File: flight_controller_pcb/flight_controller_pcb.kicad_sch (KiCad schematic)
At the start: 52 parts, among them J1 Conn_01x08, J2 Conn_01x05, J3 Conn_01x02, U1 NRF24L01P-R7, U2 TPS62162DSG, U3 STM32F411CEUx, U4 RFX2401C, U5 BMP390, U6 MPU-6500, U7 2450LP14A0100001T, Y1 Crystal_GND24

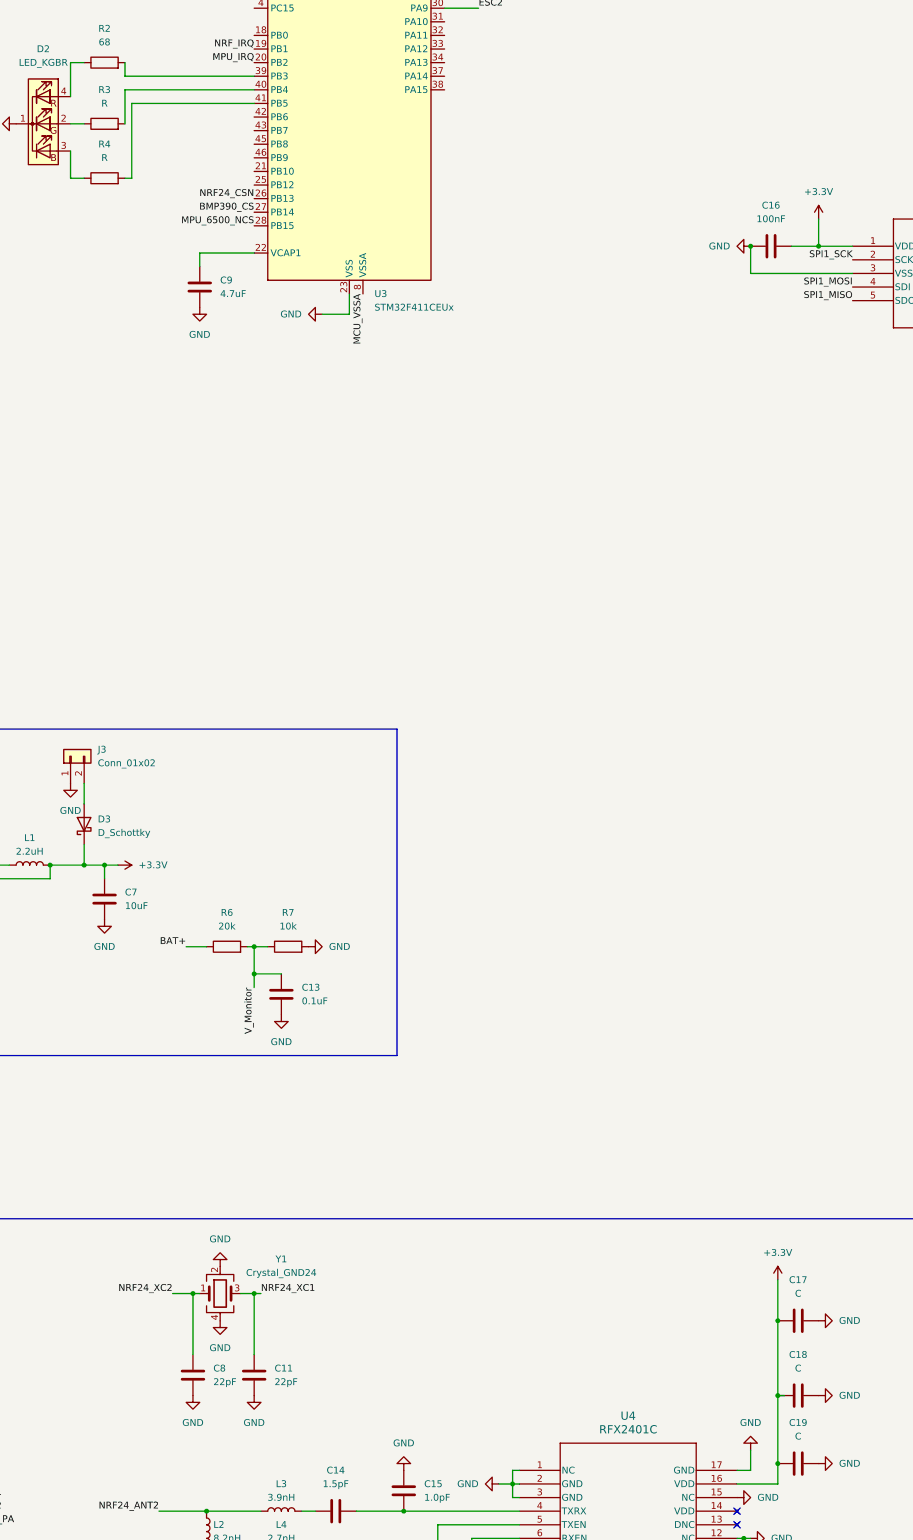
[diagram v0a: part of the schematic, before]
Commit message: assigned several footprints in FC schema
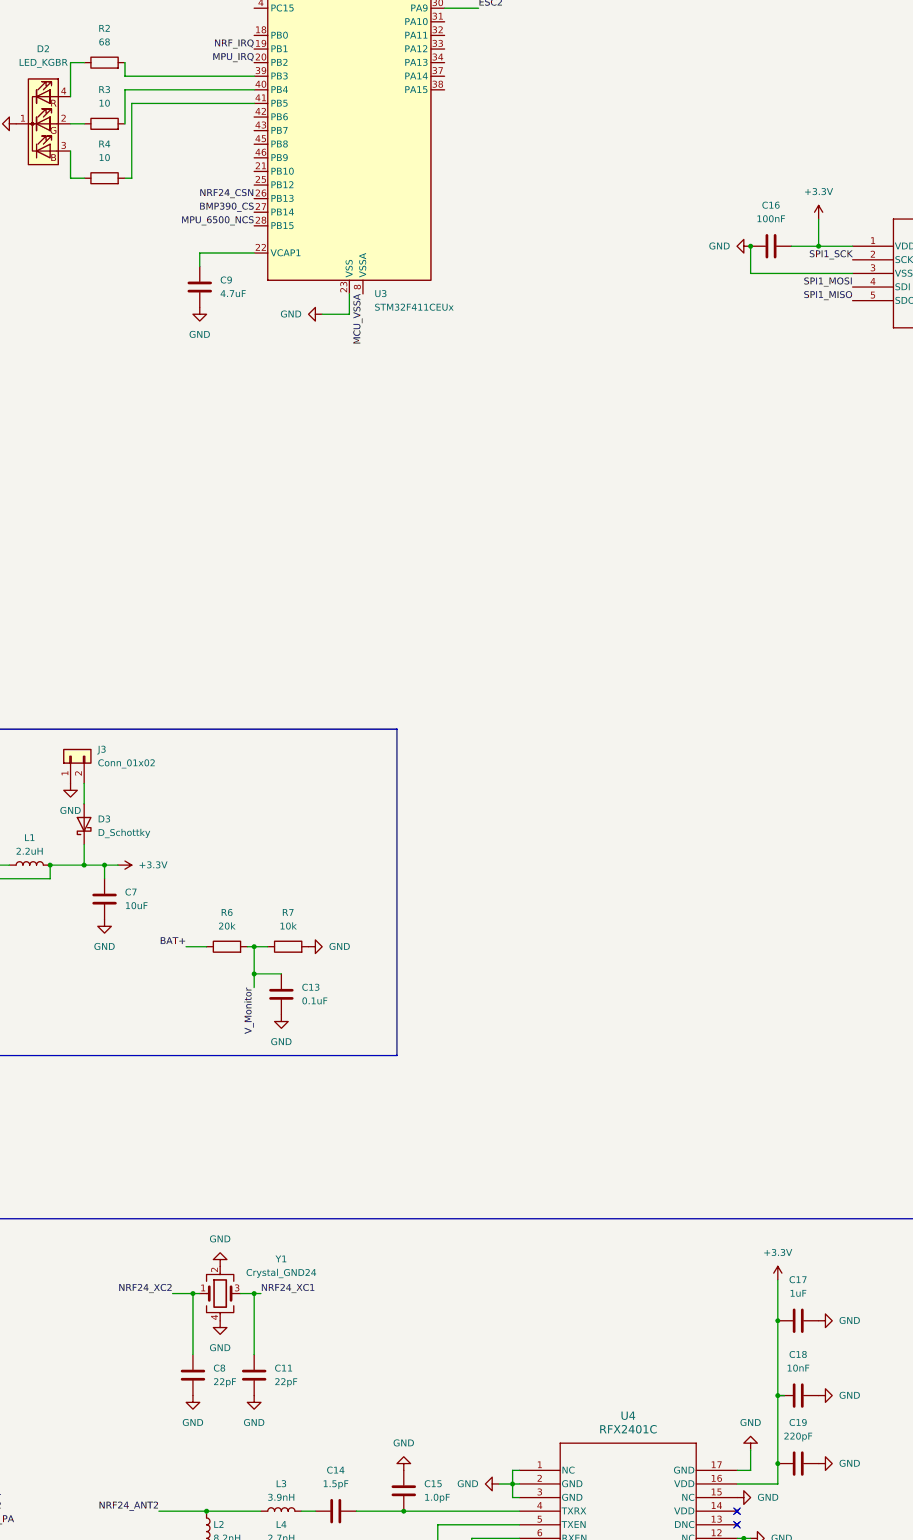
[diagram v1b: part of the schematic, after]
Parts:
- C14, C15, C5, C6: footprint (none) -> Capacitor_SMD:C_0402_1005Metric
- C17: value C -> 1uF; footprint (none) -> Capacitor_SMD:C_0402_1005Metric
- C18: value C -> 10nF; footprint (none) -> Capacitor_SMD:C_0603_1608Metric
- C19: value C -> 220pF; footprint (none) -> Capacitor_SMD:C_0402_1005Metric
- C20: footprint (none) -> Capacitor_SMD:C_0201_0603Metric
- C9: footprint (none) -> Capacitor_SMD:C_0603_1608Metric
- L3, L4: footprint (none) -> Inductor_SMD:L_0201_0603Metric
- R2, R5, R8, R9: footprint (none) -> Resistor_SMD:R_0402_1005Metric
- R3, R4: value R -> 10; footprint (none) -> Resistor_SMD:R_0402_1005Metric
- TP1: footprint (none) -> TestPoint:TestPoint_Pad_3.0x3.0mm
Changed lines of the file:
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@@
 			)
 		)
-		(property "Footprint" ""
+		(property "Footprint" "Capacitor_SMD:C_0201_0603Metric"
 			(at 229.5652 386.08 0)
 			(effects
@@
 			)
 		)
-		(property "Description" "Unpolarized capacitor"
+		(property "Description" "Unpolarized capacitor (C180283)"
 			(at 228.6 382.27 0)
 			(effects
@@
 			)
 		)
-		(property "Value" "R"
+		(property "Value" "10"
 			(at 95.25 105.41 90)
 			(effects
@@
 			)
 		)
-		(property "Footprint" ""
+		(property "Footprint" "Resistor_SMD:R_0402_1005Metric"
 			(at 95.25 110.998 90)
 			(effects
@@
 			)
 		)
-		(property "Description" "Resistor"
+		(property "Description" "Resistor (C25077)"
 			(at 95.25 109.22 0)
 			(effects
@@
 			)
 		)
-		(property "Footprint" ""
+		(property "Footprint" "TestPoint:TestPoint_Pad_3.0x3.0mm"
 			(at 290.83 383.54 0)
 			(effects
@@
 			)
 		)
-		(property "Footprint" ""
+		(property "Footprint" "Capacitor_SMD:C_0402_1005Metric"
 			(at 77.1652 50.8 0)
 			(effects
@@
 			)
 		)
-		(property "Description" "Unpolarized capacitor"
+		(property "Description" "Unpolarized capacitor (C52923)"
 			(at 76.2 46.99 0)
 			(effects
@@
 			)
 		)
-		(property "Footprint" ""
+		(property "Footprint" "Capacitor_SMD:C_0603_1608Metric"
 			(at 112.0648 135.89 0)
 			(effects
@@
 			)
 		)
-		(property "Description" "Unpolarized capacitor (MLCC, low ERS < 1ohm)"
+		(property "Description" "Unpolarized capacitor (C107368)"
 			(at 113.03 139.7 0)
 			(effects
@@
 			)
 		)
-		(property "Footprint" ""
+		(property "Footprint" "Resistor_SMD:R_0402_1005Metric"
 			(at 95.25 99.568 90)
 			(effects
@@
 			)
 		)
-		(property "Description" "Resistor"
+		(property "Description" "Resistor (C163455)"
 			(at 95.25 97.79 0)
 			(effects
@@
 			)
 		)
-		(property "Footprint" ""
+		(property "Footprint" "Resistor_SMD:R_0402_1005Metric"
 			(at 162.052 379.73 90)
 			(effects
@@
 			)
 		)
-		(property "Description" "Resistor"
+		(property "Description" "Resistor (C11702)"
 			(at 163.83 379.73 0)
 			(effects
@@
 			)
 		)
-		(property "Value" "C"
+		(property "Value" "10nF"
 			(at 224.79 341.63 90)
 			(effects
@@
 			)
 		)
-		(property "Footprint" ""
+		(property "Footprint" "Capacitor_SMD:C_0603_1608Metric"
 			(at 228.6 345.7448 0)
 			(effects
@@
 			)
 		)
-		(property "Description" "Unpolarized capacitor"
+		(property "Description" "Unpolarized capacitor (C389113)"
 			(at 224.79 346.71 0)
 			(effects
@@
 			)
 		)
-		(property "Footprint" ""
+		(property "Footprint" "Resistor_SMD:R_0402_1005Metric"
 			(at 104.902 73.66 90)
 			(effects
@@
 			)
 		)
-		(property "Description" "Resistor"
+		(property "Description" "Resistor (C25744)"
 			(at 106.68 73.66 0)
 			(effects
@@
 			)
 		)
-		(property "Footprint" ""
+		(property "Footprint" "Inductor_SMD:L_0201_0603Metric"
 			(at 128.27 375.92 0)
 			(effects
@@
 			)
 		)
-		(property "Description" "Inductor (chip inductor +/- 5%)"
+		(property "Description" "Inductor (C98043)"
 			(at 128.27 375.92 0)
 			(effects
@@
 			)
 		)
-		(property "Footprint" ""
+		(property "Footprint" "Inductor_SMD:L_0201_0603Metric"
 			(at 128.27 368.3 0)
 			(effects
@@
 			)
 		)
-		(property "Description" "Inductor"
+		(property "Description" "Inductor (C918993)"
 			(at 128.27 368.3 0)
 			(effects
@@
 			)
 		)
-		(property "Footprint" ""
+		(property "Footprint" "Capacitor_SMD:C_0402_1005Metric"
 			(at 152.0952 368.3 0)
 			(effects
@@
 			)
 		)
-		(property "Description" "Unpolarized capacitor (NPO, +/- 0.1pF)"
+		(property "Description" "Unpolarized capacitor (C309455)"
+			(at 151.13 364.49 0)
+			(effects
+				(font
+					(size 1.27 1.27)
+				)
+				(hide yes)
+			)
+		)
+		(property "Field5" ""
 			(at 151.13 364.49 0)
 			(effects
@@
 			)
 		)
-		(property "Footprint" ""
+		(property "Footprint" "Capacitor_SMD:C_0402_1005Metric"
 			(at 142.24 367.3348 0)
 			(effects
@@
 			)
 		)
-		(property "Description" "Unpolarized capacitor (NPO, +/- 0.1pF)"
+		(property "Description" "Unpolarized capacitor (C282238)"
 			(at 138.43 368.3 0)
 			(effects
@@
 			)
 		)
-		(property "Value" "R"
+		(property "Value" "10"
 			(at 95.25 115.57 90)
 			(effects
@@
 			)
 		)
-		(property "Footprint" ""
+		(property "Footprint" "Resistor_SMD:R_0402_1005Metric"
 			(at 95.25 121.158 90)
 			(effects
@@
 			)
 		)
-		(property "Description" "Resistor"
+		(property "Description" "Resistor (C25077)"
 			(at 95.25 119.38 0)
 			(effects
@@
 			)
 		)
-		(property "Footprint" ""
+		(property "Footprint" "Capacitor_SMD:C_0402_1005Metric"
 			(at 88.5952 50.8 0)
 			(effects
@@
 			)
 		)
-		(property "Description" "Unpolarized capacitor"
+		(property "Description" "Unpolarized capacitor (C15195)"
 			(at 87.63 46.99 0)
 			(effects
@@
 			)
 		)
-		(property "Description" "Inductor (C76778)"
+		(property "Description" "Inductor (C404576)"
 			(at 114.3 372.11 0)
 			(effects
@@
 			)
 		)
-		(property "Footprint" ""
+		(property "Footprint" "Resistor_SMD:R_0402_1005Metric"
 			(at 155.702 387.35 90)
 			(effects
@@
 			)
 		)
-		(property "Description" "Resistor"
+		(property "Description" "Resistor (C11702)"
 			(at 157.48 387.35 0)
 			(effects
@@
 			)
 		)
-		(property "Value" "C"
+		(property "Value" "220pF"
 			(at 224.79 354.33 90)
 			(effects
@@
 			)
 		)
-		(property "Footprint" ""
+		(property "Footprint" "Capacitor_SMD:C_0402_1005Metric"
 			(at 228.6 358.4448 0)
 			(effects
@@
 			)
 		)
-		(property "Description" "Unpolarized capacitor"
+		(property "Description" "Unpolarized capacitor (C326765)"
 			(at 224.79 359.41 0)
 			(effects
@@
 			)
 		)
-		(property "Value" "C"
+		(property "Value" "1uF"
 			(at 224.79 327.66 90)
 			(effects
@@
 			)
 		)
-		(property "Footprint" ""
+		(property "Footprint" "Capacitor_SMD:C_0402_1005Metric"
 			(at 228.6 331.7748 0)
 			(effects
@@
 			)
 		)
-		(property "Description" "Unpolarized capacitor"
+		(property "Description" "Unpolarized capacitor (C52923)"
 			(at 224.79 332.74 0)
 			(effects

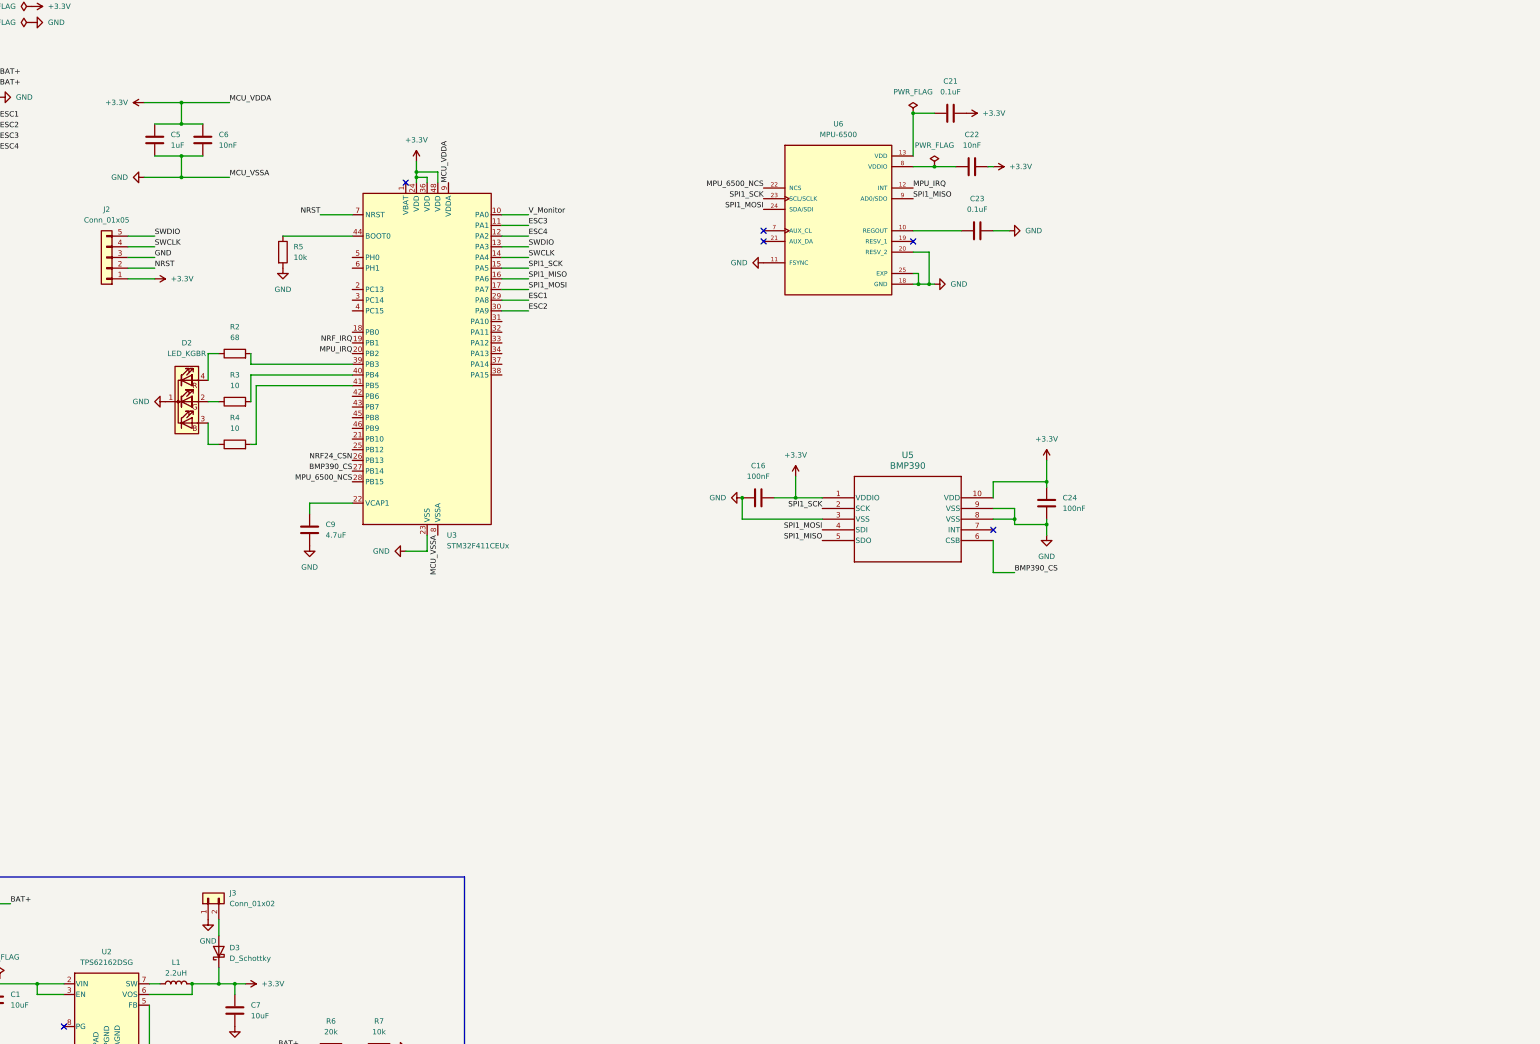
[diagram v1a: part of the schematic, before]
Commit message: Started work to replace mpu-6500 with icm-20948
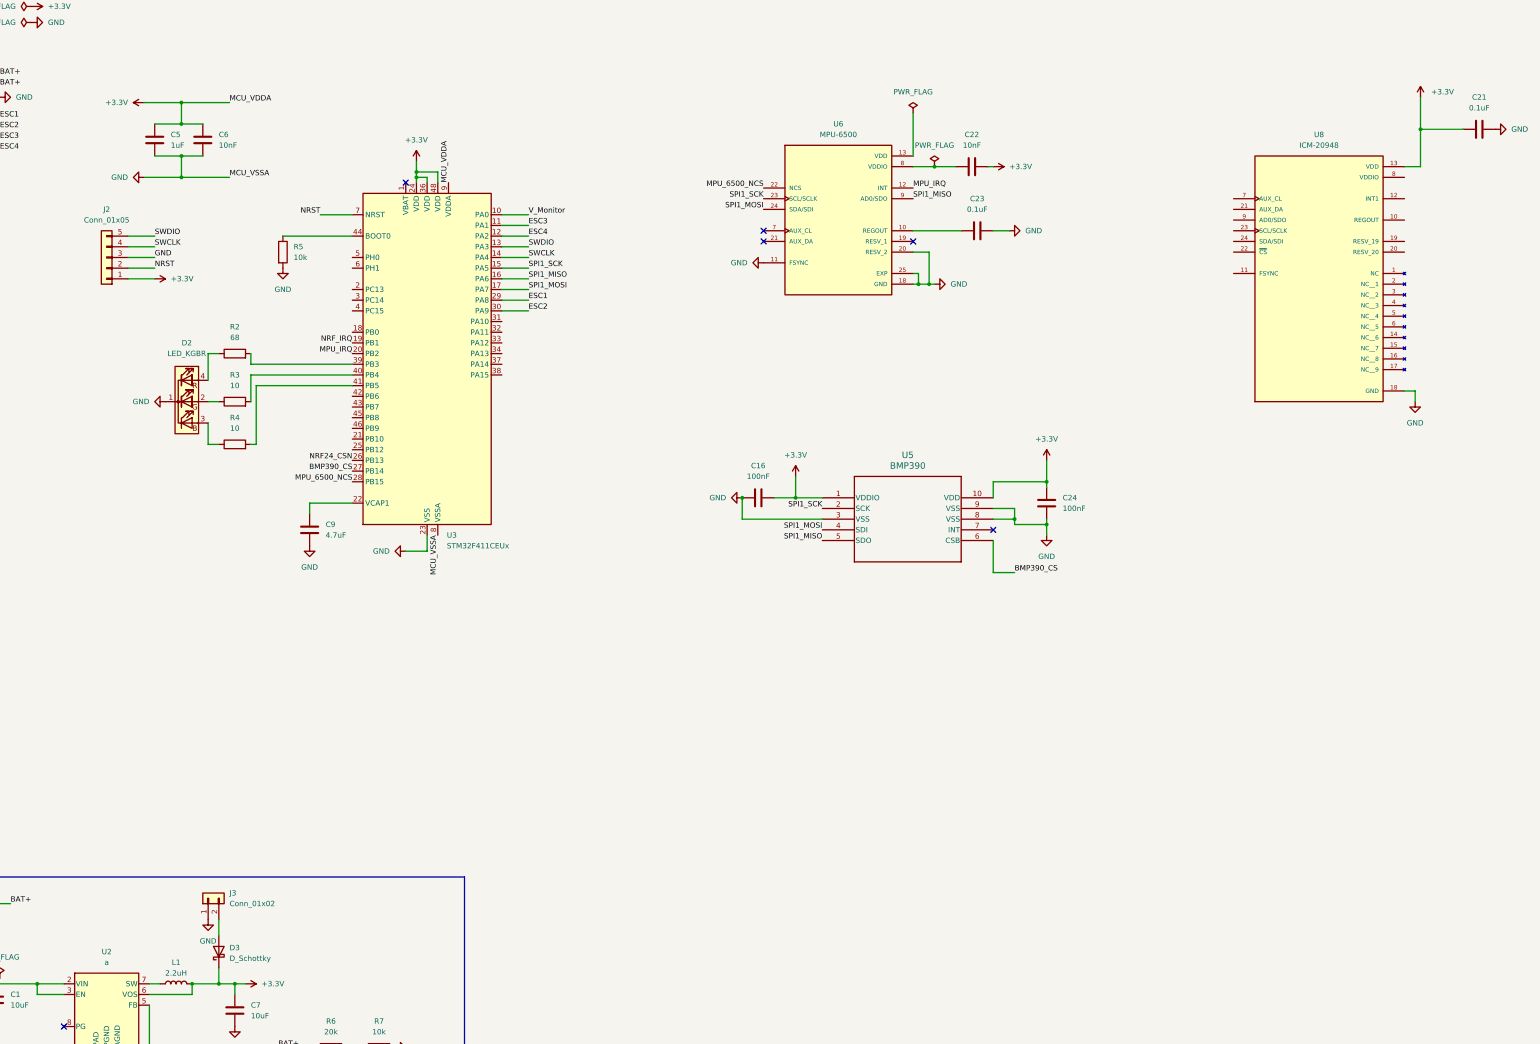
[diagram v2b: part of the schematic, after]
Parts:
- added U8: ICM-20948, ICM-20948:QFN40P300X300X105-24N, symbol ICM-20948:ICM-20948
- C16, C21, C22, C23, C24: footprint (none) -> Capacitor_SMD:C_0402_1005Metric
- U2: value TPS62162DSG -> a
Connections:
- net +3.3V: now also C21.1, U8.13 (VDD); no longer C21.2
- net GND: now also C21.2, U8.18 (GND)
- net at U6.13 (VDD): no longer C21.1
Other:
- moved on the sheet: C21

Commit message: tons of work on radio communication between controller and fc
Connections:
- net NRF24_CE: now also U3.25 (PB12)
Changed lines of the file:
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@@
+		)
+	)
+	(label "NRF24_CE"
+		(at 123.19 120.65 180)
+		(effects
+			(font
+				(size 1.27 1.27)
+			)
+			(justify right bottom)
 		)
 	)
